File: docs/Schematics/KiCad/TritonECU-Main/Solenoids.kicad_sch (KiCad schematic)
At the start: 46 parts, among them Q401 NCV8405ASTT1G, Q402 NCV8405ASTT1G, Q403 NCV8405ASTT1G, Q404 NCV8405ASTT1G, Q405 NCV8405ASTT1G, Q406 NCV8405ASTT1G, Q407 NCV8405ASTT1G, Q408 NCV8405ASTT1G, U401 74HCT541, U402 74HC4051

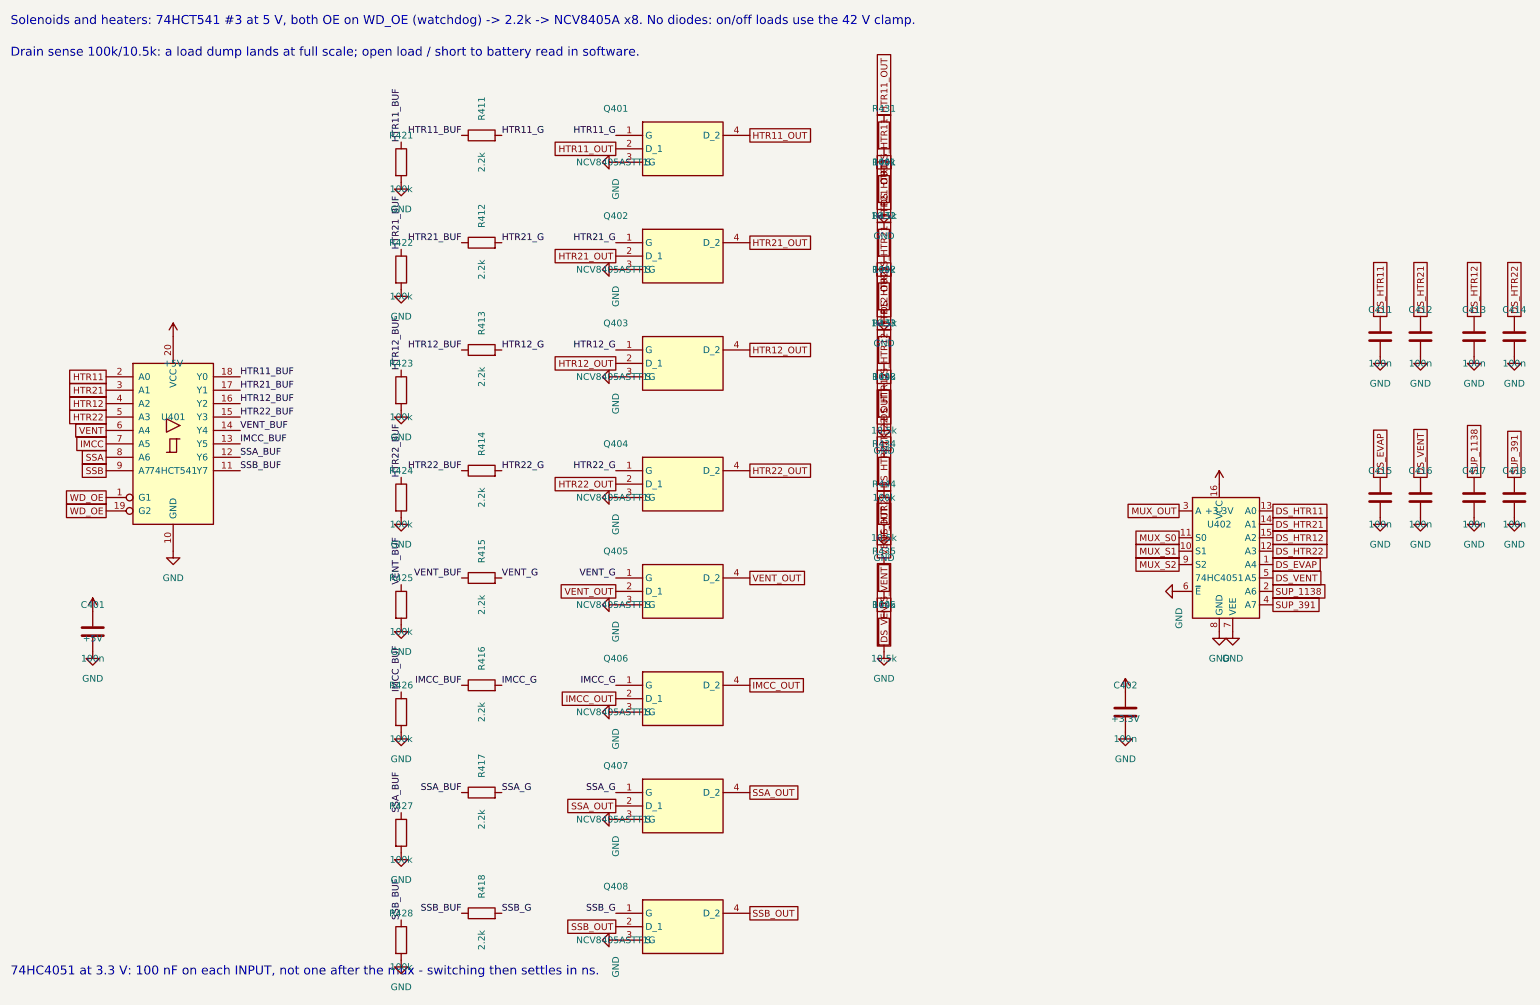
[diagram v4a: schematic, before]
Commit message: Carrier: Inputs sheet and switched rails for sleep
Inputs: one network per switch input - 4.7k pull-up to VPWR (ground-
switched only; VPWR so a TR bit closed in Park draws nothing parked),
SMF24A, 33k/15k, 10n, BAT54J to 3.3 V. TR1/2/4 and 4X4L ground-switched,
TR3A/BRAKE/ACP/TCS 12 V high-side. 4X4L mapped to EEC-V pin 14
(findings sec.14). IGN_WAKE from VPWR into PC13/WKUP4. TACH/SPEED bench
header, BOOT0 DFU solder jumper.

Switched rails: +5V and +3.3V stay up parked, so two TPS22917 load
switches on SW_RAIL_EN (PG12, 100k down) make +5V_SW / +3.3V_SW for the
running-only loads: 74HCT541 x3 and OE pull-ups, MAX9926 x3 and COUT
pull-ups, ADS8588H, OPA2376 x2, O2 bias, knock block, 74HC4051, TPS2H160B
FAULT pull-up, TFT pull-up. MCU, watchdog, CAN, SCP RX, clamps stay on.

gen_carrier_pcb.py: packer steps around existing parts, fills several
rects in turn, parks overflow below earlier parked parts.

Co-Authored-By: Claude Opus 5.5 <noreply@anthropic.com>
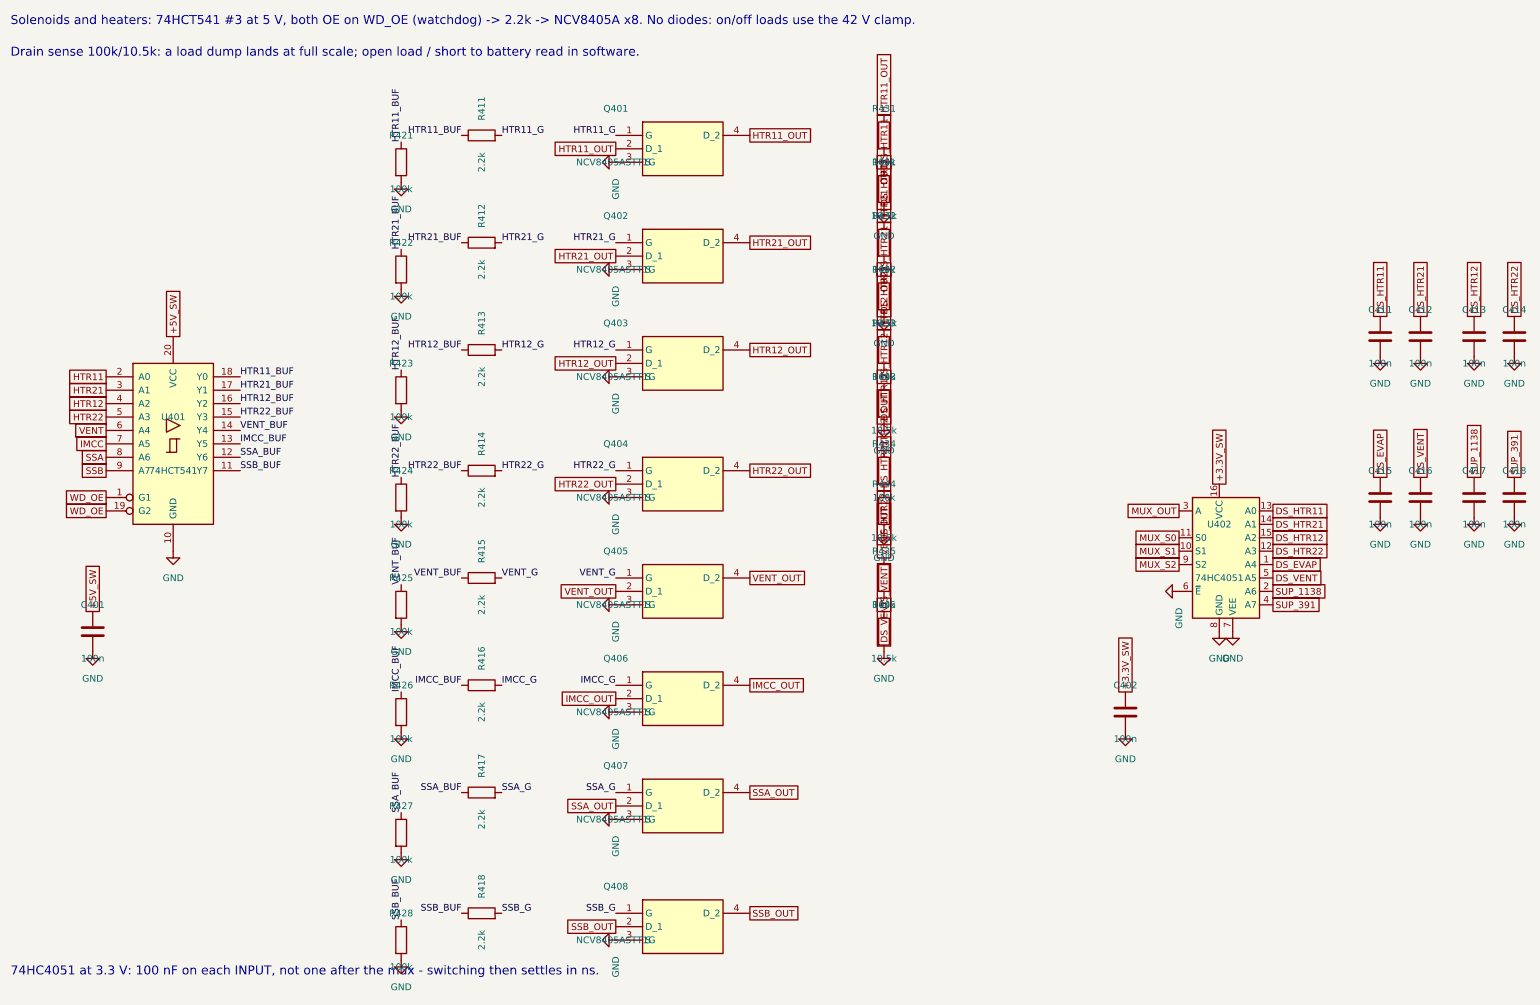
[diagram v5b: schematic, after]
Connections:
- net +3.3V renamed +3.3V_SW
- net +5V renamed +5V_SW
